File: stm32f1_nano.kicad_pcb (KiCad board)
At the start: 2 copper layers, 43.2 x 17.8 mm, 52 parts, among them J1 Analog, J2 Digital, J3 TYPE-C-31-M-12, J4 Conn_ST_STDC14, Q1 AO3401A, Q3 AO3401A, U1 STM32F103C8T6, U2 W25Q32JVSS, U3 AMS1117-3.3, U5 AMS1117-5.0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

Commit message: First draft almost done
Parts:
- removed C12: 100n 16V, Capacitor_SMD:C_0402_1005Metric
- removed C15, C16: 22u 25V, Capacitor_SMD:C_0805_2012Metric
- removed D7: 6V, Diode_SMD:D_MiniMELF
- removed J4: Conn_ST_STDC14, Project_Library:Samtec_FTSH-107-XX-YYY-DV-K-A
- removed JP2: Disc. 12V PS, Jumper:SolderJumper-2_P1.3mm_Bridged_RoundedPad1.0x1.5mm
- removed Q3: AO3401A, Package_TO_SOT_SMD:SOT-23
- removed R11: 100k, Resistor_SMD:R_0402_1005Metric
- removed U2: W25Q32JVSS, Package_SO:SOIC-8_5.23x5.23mm_P1.27mm
- removed U5: AMS1117-5.0, Package_TO_SOT_SMD:SOT-223-3_TabPin2
- added J5: DEBUG, Connector_PinHeader_2.54mm:PinHeader_1x04_P2.54mm_Vertical, F.Cu at (141.5, 87.3)
- moved D5 93.0 mm to (133.7, 93.8), turned to 180 degrees
- moved R10 87.2 mm to (132.0, 95.4)
- moved Q1 84.6 mm to (129.2, 94.5), turned to -90 degrees
- moved U3 77.4 mm to (131.6, 89.0), turned to 180 degrees
- moved C14 74.6 mm to (137.8, 85.5)
- moved C13 74.4 mm to (134.7, 95.9), turned to 180 degrees
- moved D6 12.0 mm to (110.5, 86.8)
- moved R9 11.3 mm to (108.5, 86.5), turned to -90 degrees
- moved C8 8.89 mm to (113.2, 94.7), turned to 180 degrees
- moved C1 7.24 mm to (126.7, 95.8)
- moved D4 6.38 mm to (138.0, 94.9)
- moved D3 6.34 mm to (138.0, 87.3), turned to 180 degrees
- moved D1 6.29 mm to (138.0, 92.4)
- moved D2 6.28 mm to (138.0, 89.8)
- moved R4 4.82 mm to (138.0, 96.2), turned to 180 degrees
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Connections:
- J2 pad 13: /~{RESET} -> unconnected-(J2-Pin_13-Pad13)
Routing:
- net GND: track 44.8 -> 128.6 mm, vias 1 -> 4
- net VBUS: track 0.00 -> 31.6 mm, vias 0 -> 3
- net +5V: track 0.00 -> 25.5 mm, vias 0 -> 1
- net +3.3V: track 55.8 -> 77.0 mm, vias 2 -> 0
- net /~{RESET}: track 42.5 -> 24.7 mm, vias 2 -> 1
- net SWDIO: track 13.0 -> 27.4 mm, vias 2 -> 1
- net /LED1_GRN: track 16.7 -> 29.2 mm
- net /LED3_RED: track 17.8 -> 27.6 mm
- net /LED2_ORG: track 9.41 -> 16.2 mm
- net /LED4_BLU: track 9.79 -> 16.3 mm
- net /PA10: track 25.6 -> 19.2 mm
- net /PB8: track 9.43 -> 15.0 mm
- net /PB6: track 13.7 -> 17.5 mm
- net Net-(D5-A): track 0.00 -> 3.64 mm
- net /USB_D-: track 22.5 -> 25.8 mm
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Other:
- board text removed: "USB Mini-B"

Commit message: New PS
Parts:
- removed C13, C14: 22u 25V, Capacitor_SMD:C_0805_2012Metric
- removed D5: 6V, Diode_SMD:D_MiniMELF
- removed D6: LED red (PWR), LED_SMD:LED_0603_1608Metric
- removed JP1: Disc. VBUS, Jumper:SolderJumper-2_P1.3mm_Bridged_RoundedPad1.0x1.5mm
- removed Q1: AO3401A, Package_TO_SOT_SMD:SOT-23
- removed R10: 100k, Resistor_SMD:R_0402_1005Metric
- removed R9: 1k5, Resistor_SMD:R_0402_1005Metric
- removed U3: AMS1117-3.3, Package_TO_SOT_SMD:SOT-223-3_TabPin2
- added C12: 100n 16V, Capacitor_SMD:C_0402_1005Metric, B.Cu at (63.6, 88.6)
- added C15: 22u 25V, Capacitor_SMD:C_0805_2012Metric, B.Cu at (72.1, 72.1)
- added C16: 22u 25V, Capacitor_SMD:C_0805_2012Metric, B.Cu at (72.1, 75.9)
- added C17: 1u 25V, Capacitor_SMD:C_0402_1005Metric, F.Cu at (110.5, 92.8)
- added C18: 1u 25V, Capacitor_SMD:C_0402_1005Metric, F.Cu at (108.9, 87.7)
- added D7: 6V, Diode_SMD:D_MiniMELF, B.Cu at (72.1, 84.8)
- added D8: LED red (PWR), LED_SMD:LED_0603_1608Metric, F.Cu at (109.7, 86.4)
- added D9: 1N5819WS, Diode_SMD:D_SOD-323, F.Cu at (109.7, 94.4)
- added JP2: Disc. 12V PS, Jumper:SolderJumper-2_P1.3mm_Bridged_RoundedPad1.0x1.5mm, B.Cu at (72.7, 79.7)
- added Q3: AO3401A, Package_TO_SOT_SMD:SOT-23, B.Cu at (77.1, 75.9)
- added R11: 100k, Resistor_SMD:R_0402_1005Metric, B.Cu at (71.5, 88.6)
- added R12: 1k5, Resistor_SMD:R_0402_1005Metric, F.Cu at (110.8, 87.7)
- added U2: W25Q32JVSS, Package_SO:SOIC-8_5.23x5.23mm_P1.27mm, B.Cu at (63.2, 83.5)
- added U4: XC6206P332MR, Package_TO_SOT_SMD:SOT-23-3, F.Cu at (109.7, 90.2)
- added U5: AMS1117-5.0, Package_TO_SOT_SMD:SOT-223-3_TabPin2, B.Cu at (64.4, 74.6)
- moved X1 21.5 mm to (132.9, 89.0), turned to -90 degrees
- moved C11 20.7 mm to (129.7, 86.8), turned to -90 degrees
- moved C10 15.2 mm to (129.7, 89.8), turned to 90 degrees
- moved C9 13.7 mm to (127.9, 86.0), turned to 0 degrees
- moved C1 13.5 mm to (115.7, 87.9), turned to 45 degrees
- moved C5 11.9 mm to (128.3, 92.9), turned to -135 degrees
- moved C3 11.8 mm to (119.8, 96.8), turned to 135 degrees
- moved C6 11.6 mm to (125.5, 86.5), turned to -45 degrees
- moved C2 11.6 mm to (116.5, 88.7), turned to 45 degrees
- moved R5 10.8 mm to (126.9, 94.3), turned to 45 degrees
- moved C4 10.7 mm to (127.7, 88.7), turned to 135 degrees
- moved L1 8.72 mm to (113.1, 86.2), turned to 180 degrees
- moved C8 6.81 mm to (112.2, 87.9), turned to -90 degrees
- moved C7 6.11 mm to (115.4, 86.3), turned to -90 degrees
- moved R8 5.35 mm to (108.9, 96.4), turned to 0 degrees
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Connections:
- net Net-(JP1-B) renamed /VBUS0
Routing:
- net GND: track 128.6 -> 32.7 mm, vias 4 -> 6
- net +3.3V: track 77.0 -> 38.2 mm, vias 0 -> 1
- net VBUS: track 31.6 -> 0.00 mm, vias 3 -> 0
- net /PB14: track 30.3 -> 0.00 mm, vias 1 -> 0
- net /LED1_GRN: track 29.2 -> 0.00 mm, vias 2 -> 0
- net /PB13: track 28.3 -> 0.00 mm, vias 1 -> 0
- net /LED3_RED: track 27.6 -> 0.00 mm
- net SWDIO: track 27.4 -> 0.00 mm, vias 1 -> 0
- net /PB15: track 26.2 -> 0.00 mm, vias 1 -> 0
- net /PB12: track 25.4 -> 0.00 mm, vias 1 -> 0
- net /~{RESET}: track 24.7 -> 0.00 mm, vias 1 -> 0
- net SWO: track 22.2 -> 0.00 mm, vias 1 -> 0
- net +5V: track 25.5 -> 3.49 mm, vias 1 -> 0
- net /PA9: track 20.8 -> 0.00 mm, vias 1 -> 0
- net SWCLK: track 20.2 -> 0.00 mm, vias 1 -> 0
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- added copper zone on B.Cu, net GND

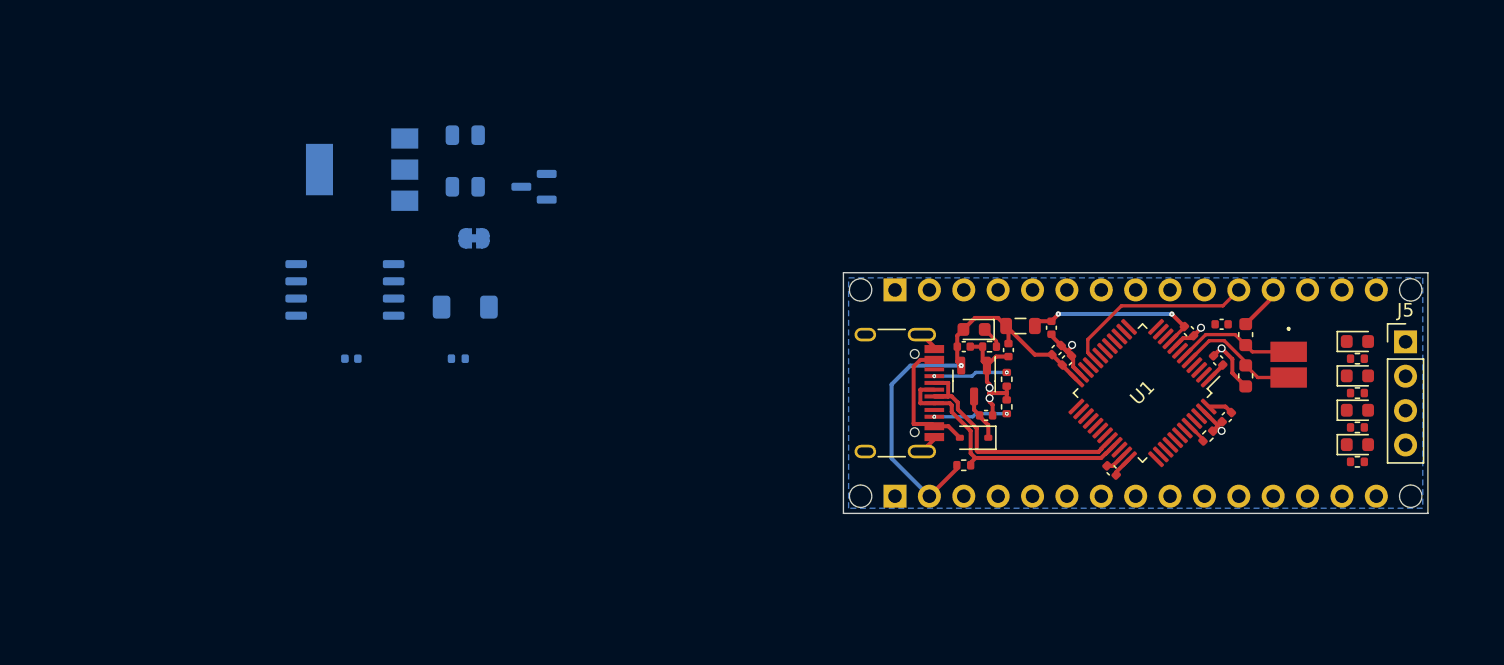
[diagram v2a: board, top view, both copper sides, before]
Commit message: Reassigned Pins
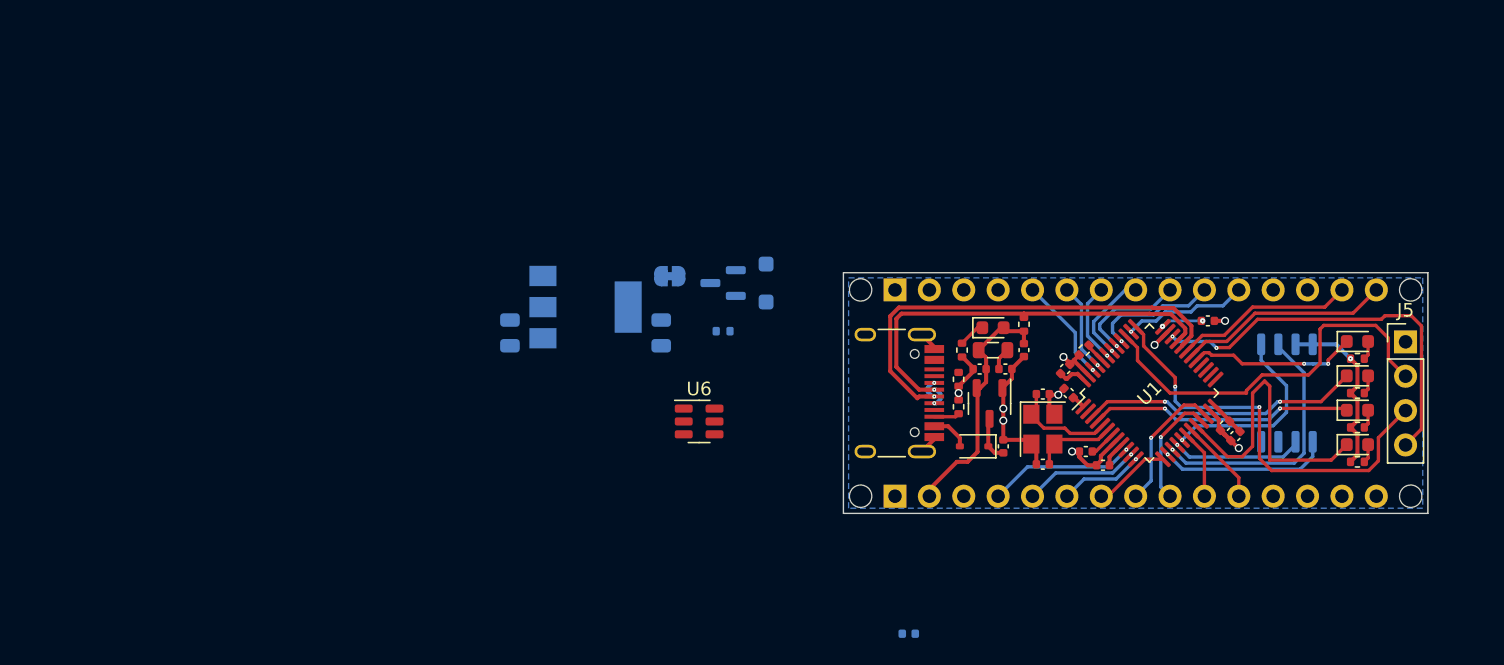
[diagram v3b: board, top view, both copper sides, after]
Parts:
- removed C11: 20p 50V, Capacitor_SMD:C_0603_1608Metric
- removed D7: 6V, Diode_SMD:D_MiniMELF
- removed X1: NX3225GD-8MHZ-STD-CRA-3, Project_Library:NX3225GD8MHZSTDCRA3
- added C19: 20p 50V, Capacitor_SMD:C_0402_1005Metric, F.Cu at (114.7, 91.2)
- added D10: SMF6.0CA, Diode_SMD:D_SOD-123F, B.Cu at (94.3, 83.0)
- added U6: SRV05-4, Package_TO_SOT_SMD:SOT-23-6, F.Cu at (89.3, 93.2)
- added Y1: X322516MLB4SI, Crystal:Crystal_SMD_3225-4Pin_3.2x2.5mm, F.Cu at (114.7, 93.8)
- C10: footprint Capacitor_SMD:C_0603_1608Metric -> Capacitor_SMD:C_0402_1005Metric
- moved U2 70.0 mm to (132.8, 91.1), turned to 90 degrees
- moved C12 45.9 mm to (104.8, 108.9)
- moved R11 19.7 mm to (91.1, 86.5)
- moved U5 19.4 mm to (81.0, 84.8), turned to 0 degrees
- moved C16 18.1 mm to (86.5, 86.7), turned to -90 degrees
- moved C10 16.3 mm to (114.7, 96.4), turned to 0 degrees
- moved Q3 15.7 mm to (91.1, 83.0)
- moved C15 15.0 mm to (75.4, 86.7), turned to -90 degrees
- moved JP2 14.7 mm to (87.2, 82.5), turned to 0 degrees
- moved C1 14.7 mm to (129.0, 94.3), turned to -135 degrees
- moved C9 13.7 mm to (117.9, 95.4), turned to 180 degrees
- moved C3 13.1 mm to (126.9, 85.8), turned to 0 degrees
- moved C2 12.6 mm to (128.2, 93.5), turned to -135 degrees
- moved C5 12.5 mm to (116.4, 89.3), turned to 45 degrees
- moved C6 11.8 mm to (119.2, 96.4), turned to 180 degrees
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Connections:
- C10 pad 2: /HSE_IN -> /HSE_OUT
- J1 pad 8: /PB7 -> /PB11
- J1 pad 9: /PB6 -> /PB10
- J2 pad 10: /PA8 -> /PB4
- J2 pad 11: /PB2 -> /PA15
- J2 pad 4: /PB9 -> /PC13
- J2 pad 5: /PB8 -> /PB9
- J2 pad 6: /PC14 -> /PB8
- J2 pad 7: /PC13 -> /PB7
- J2 pad 8: /PB5 -> /PB6
- J2 pad 9: /PB4 -> /PB5
- U1 pad 20: /PB2 -> /LED4_BLU
- U1 pad 21: /LED3_RED -> /PB10
- U1 pad 22: /LED4_BLU -> /PB11
- U1 pad 29: /PA8 -> /LED3_RED
- U1 pad 3: /PC14 -> /LED2_ORG
- U1 pad 38: /LED2_ORG -> /PA15
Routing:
- net SWCLK: track 0.00 -> 30.9 mm, vias 0 -> 2
- net SWDIO: track 0.00 -> 29.3 mm, vias 0 -> 2
- net SWO: track 0.00 -> 29.0 mm
- net /LED4_BLU: track 0.00 -> 22.8 mm
- net /LED2_ORG: track 0.00 -> 20.7 mm, vias 0 -> 2
- net /LED1_GRN: track 0.00 -> 19.5 mm, vias 0 -> 2
- net /SPI1_SCK: track 0.00 -> 19.3 mm, vias 0 -> 1
- net /PA9: track 0.00 -> 15.7 mm
- net /USB_D-: track 19.4 -> 34.6 mm, vias 0 -> 2
- net /PB2: track 14.5 -> 0.00 mm
- net /SPI1_MOSI: track 0.00 -> 14.4 mm, vias 0 -> 1
- net /PA10: track 0.00 -> 13.3 mm
- net /SPI1_NSS: track 0.00 -> 12.6 mm, vias 0 -> 1
- net /LED3_RED: track 0.00 -> 12.5 mm, vias 0 -> 2
- net /USB_D+: track 20.4 -> 32.1 mm, vias 0 -> 2
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
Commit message: Almost done
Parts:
- removed D10: SMF6.0CA, Diode_SMD:D_SOD-123F
- removed JP2: Disc. 12V PS, Jumper:SolderJumper-2_P1.3mm_Bridged_RoundedPad1.0x1.5mm
- removed Q3: AO3401A, Package_TO_SOT_SMD:SOT-23
- removed R11: 100k, Resistor_SMD:R_0402_1005Metric
- removed U6: SRV05-4, Package_TO_SOT_SMD:SOT-23-6
- C12: value 100n 16V -> 100nF 16V
- C15, C16: moved to F.Cu
- U2: value W25Q32JVSS -> W25Q128JVSIQ
- moved C15 56.8 mm to (131.5, 95.6), turned to 0 degrees
- moved U5 52.4 mm to (132.8, 92.4), turned to 90 degrees
- moved C16 48.0 mm to (134.1, 93.5), turned to 0 degrees
- moved U2 20.3 mm to (112.7, 93.9), turned to 0 degrees
- moved C12 16.0 mm to (107.5, 93.1), turned to 90 degrees
- moved R12 5.84 mm to (114.6, 87.8), turned to 0 degrees
- moved C8 4.83 mm to (108.5, 88.2)
- moved D8 2.54 mm to (113.6, 86.3), turned to 180 degrees
- moved R8 2.44 mm to (110.9, 86.4), turned to 180 degrees
- moved R5 1.28 mm to (116.5, 87.8), turned to 180 degrees
- moved C1 0.72 mm to (129.5, 93.8)
- moved C2 0.72 mm to (128.7, 93.0)
- moved C6 0.18 mm to (119.0, 96.3)
- moved L1 0.13 mm to (110.9, 87.9)
- moved C9 0.13 mm to (117.9, 95.3)
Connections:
- net /VBUS0 renamed VBUS
- C16 pad 1: Net-(JP2-A) -> +5V
- U5 pad 2: Net-(JP2-A) -> +5V
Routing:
- net +3.3V: track 40.7 -> 85.5 mm, vias 3 -> 2
- net /PB13: track 0.00 -> 37.8 mm, vias 0 -> 2
- net +5V: track 3.38 -> 36.6 mm, vias 0 -> 1
- net /PB15: track 0.00 -> 26.6 mm, vias 0 -> 2
- net /PB14: track 0.00 -> 26.3 mm, vias 0 -> 2
- net /PB12: track 0.00 -> 23.4 mm, vias 0 -> 2
- net /~{RESET}: track 1.95 -> 22.5 mm
- net +3.3VA: track 3.53 -> 20.1 mm
- net /PC13: track 0.00 -> 16.3 mm, vias 0 -> 2
- net GND: track 34.5 -> 46.6 mm, vias 9 -> 10
- net +12V: track 0.00 -> 10.3 mm, vias 0 -> 1
- net /SPI1_SCK: track 19.3 -> 9.11 mm
- net /SPI1_MISO: track 9.69 -> 17.6 mm
- net VBUS: track 2.87 -> 10.4 mm
- net /LED4_BLU: track 22.8 -> 17.7 mm
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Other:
- board text added: "1"
- board text added: "10"
- board text added: "11"
- board text added: "15"
- board text added: "5"
- board text added: "CLK"
- board text added: "DIO"
- board text added: "GND"
- board text added: "PB12"
- board text added: "PB14"
- board text added: "PB15"
- board text added: "PB9"
- board text added: "PC13"
- board text added: "SWO"

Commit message: First Version released to production
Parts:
- removed R12: 1k5, Resistor_SMD:R_0402_1005Metric
- added R11: 75, Resistor_SMD:R_0402_1005Metric, F.Cu at (138.0, 93.7)
- C12: value 100nF 16V -> 100n 16V
- R1, R2, R3: value 1k5 -> 300
- R4: value 1k5 -> 75
- moved R1 24.1 mm to (114.6, 87.8)
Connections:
- R1 pad 1: Net-(D1-A) -> GND
- R1 pad 2: +3.3V -> Net-(D8-K)
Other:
- board text added: "3V3"
- board text added: "5V"
- board text added: "9"
- board text added: "B"
- board text added: "G"
- board text added: "N/C"
- board text added: "O"
- board text added: "PA0"
- board text added: "PA1"
- board text added: "PA10"
- board text added: "PA15"
- board text added: "PA2"
- board text added: "PA3"
- board text added: "PA9"
- board text added: "PB0"
- board text added: "PB1"
- board text added: "PB10"
- board text added: "PB11"
- board text added: "PB13"
- board text added: "PB4"
- board text added: "PB5"
- board text added: "PB6"
- board text added: "PB7"
- board text added: "PB8"
- board text added: "R"
- board text added: "STM32F1 Nano"
- board text added: "V_{IN}"
- board text added: "easy-smart.ch"
- board text added: "easy-smart.ch STM32F1 Nano v1.0"
- board text added: "~{RST}"
- board text removed: "11"

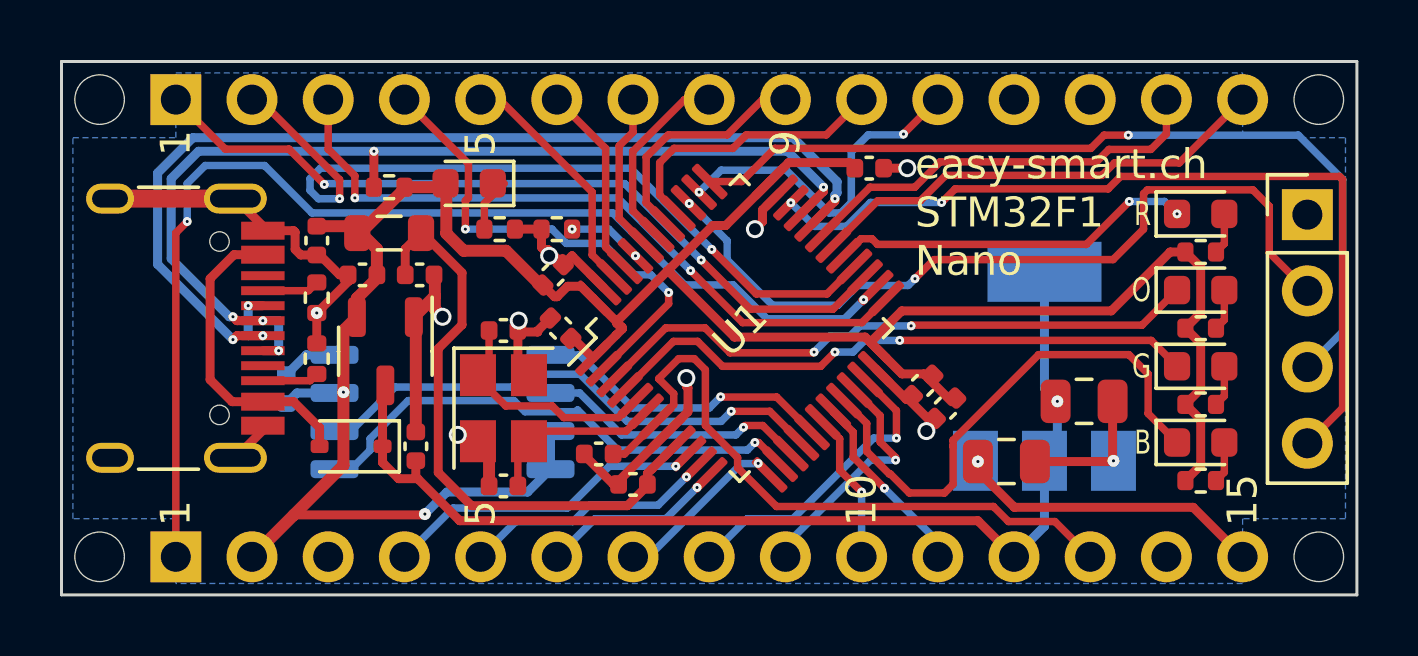
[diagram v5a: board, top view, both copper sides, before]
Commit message: Corrected distance drill-to-drill and drill-to-track
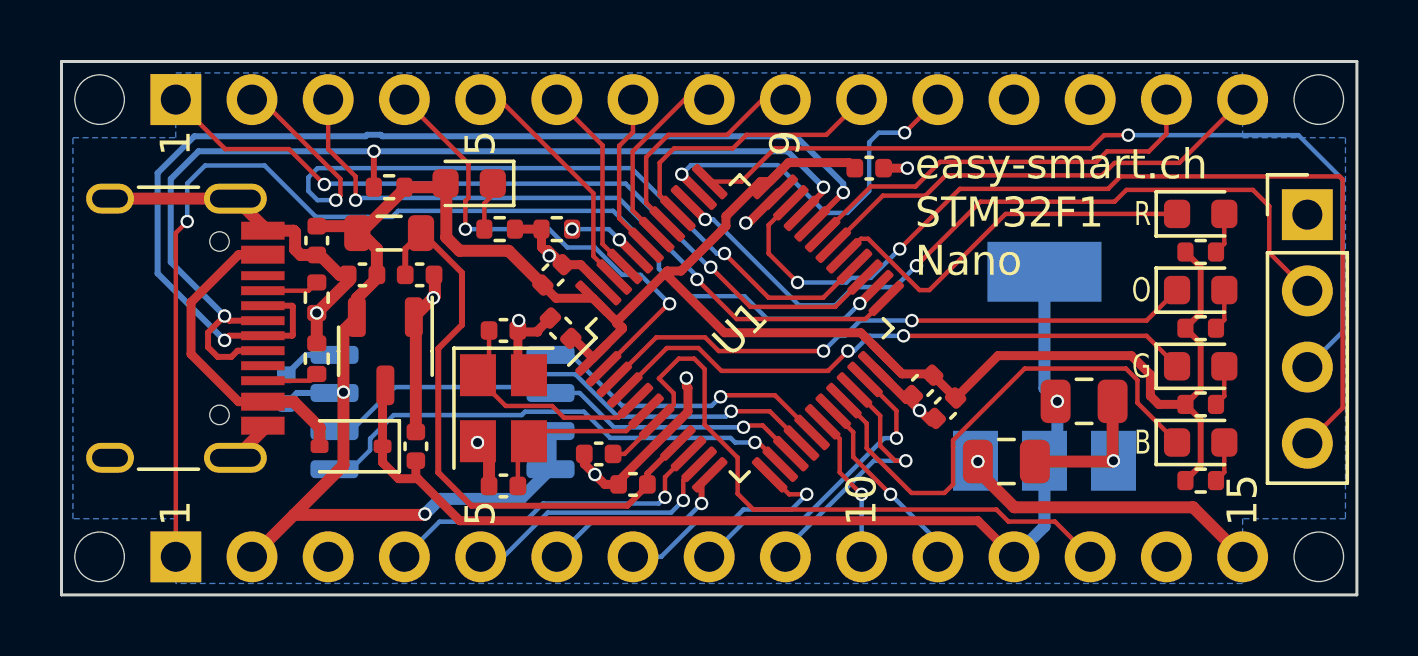
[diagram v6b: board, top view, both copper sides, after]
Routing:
- net +3.3V: track 85.5 -> 81.6 mm
- net SWDIO: track 28.7 -> 32.3 mm
- net /PA3: track 5.46 -> 8.16 mm
- net GND: track 46.6 -> 44.2 mm, vias 10 -> 11
- net SWO: track 27.0 -> 25.2 mm
- net /USB_D-: track 35.1 -> 36.7 mm, vias 4 -> 2
- net /USB_D+: track 33.6 -> 35.0 mm, vias 5 -> 3
- net /SPI1_NSS: track 17.2 -> 16.0 mm
- net /HSE_OUT: track 5.96 -> 4.96 mm
- net /PA1: track 7.96 -> 8.96 mm
- net /PA2: track 5.63 -> 6.63 mm
- net /PA0: track 10.3 -> 11.3 mm
- net /LED3_RED: track 12.2 -> 13.1 mm, vias 2 -> 0
- net +5V: track 36.6 -> 35.7 mm
- net /LED4_BLU: track 17.7 -> 16.9 mm
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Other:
- board text added: "easy-smart.ch STM32F1 Nano v1.0.1"
- board text removed: "easy-smart.ch STM32F1 Nano v1.0"
